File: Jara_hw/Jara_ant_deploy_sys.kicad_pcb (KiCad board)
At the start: 2 copper layers, 80 x 80 mm, 16 parts, among them J2 Conn_01x15, J3 Conn_01x10, Q1 Q_NMOS_GSD, Q2 Q_NMOS_GSD, SW3 SW_SPDT_312, SW4 SW_SPDT_312, U2 RFM95W-868S2

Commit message: Jennie and Jára PCBs prepared for manufacturing(?)
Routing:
- net (no net): vias 14 -> 17
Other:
- board text added: "NDE-JARA-ANT-DEPL-MECH:BOTTOM"
- board text added: "NDE-JARA-ANT-DEPL-MECH:TOP"
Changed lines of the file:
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@@
 		(pad_to_mask_clearance 0)
 		(allow_soldermask_bridges_in_footprints no)
+		(aux_axis_origin 114 54)
 		(pcbplotparams
 			(layerselection 0x00010fc_ffffffff)
@@
 			)
 		)
+		(model "C:/Users/Uživatel/Documents/MPA-NDE/kicad_project_libs/moment_switch/ZMA00A080L04RC.stp"
+			(offset
+				(xyz 0 0 0)
+			)
+			(scale
+				(xyz 1 1 1)
+			)
+			(rotate
+				(xyz 0 0 0)
+			)
+		)
 	)
 	(footprint "Connector_PinHeader_2.54mm:PinHeader_1x10_P2.54mm_Vertical"
@@
 			)
 		)
+		(model "C:/Users/Uživatel/Documents/MPA-NDE/kicad_project_libs/moment_switch/ZMA00A080L04RC.stp"
+			(offset
+				(xyz 0 0 0)
+			)
+			(scale
+				(xyz 1 1 1)
+			)
+			(rotate
+				(xyz 0 0 0)
+			)
+		)
 	)
 	(footprint "Package_TO_SOT_SMD:SOT-23"
@@
 			)
 		)
+		(model "C:/Users/Uživatel/Documents/MPA-NDE/kicad_project_libs/hoperf95/RFM95 LoRa v15.step"
+			(offset
+				(xyz 8 -8 0)
+			)
+			(scale
+				(xyz 1 1 1)
+			)
+			(rotate
+				(xyz -90 0 -180)
+			)
+		)
 	)
 	(footprint "Resistor_SMD:R_0805_2012Metric"
@@
 	)
 	(gr_line
+		(start 195.36 135.35)
+		(end 195.36 130.83)
+		(stroke
+			(width 0.6)
+			(type default)
+		)
+		(layer "Dwgs.User")
+	)
+	(gr_line
 		(start 149.6 102.25)
 		(end 147.85 102.99)
@@
 	)
 	(gr_line
+		(start 114.62 130.64)
+		(end 114.62 135.39)
+		(stroke
+			(width 0.6)
+			(type default)
+		)
+		(layer "Dwgs.User")
+	)
+	(gr_line
 		(start 147.85 102.99)
 		(end 147.33 103.07)
@@
 	)
 	(gr_line
+		(start 195.39 54.62)
+		(end 190.87 54.62)
+		(stroke
+			(width 0.6)
+			(type default)
+		)
+		(layer "Dwgs.User")
+	)
+	(gr_line
 		(start 194.49 87.16)
 		(end 194.97 87.16)
@@
 	)
 	(gr_line
+		(start 114.62 135.39)
+		(end 119.14 135.39)
+		(stroke
+			(width 0.6)
+			(type default)
+		)
+		(layer "Dwgs.User")
+	)
+	(gr_line
 		(start 162.1 117.8)
 		(end 160.43 114.67)
@@
 	)
 	(gr_line
+		(start 190.61 135.35)
+		(end 195.36 135.35)
+		(stroke
+			(width 0.6)
+			(type default)
+		)
+		(layer "Dwgs.User")
+	)
+	(gr_line
 		(start 165.08 121.54)
 		(end 162.1 117.8)
@@
 	)
 	(gr_line
+		(start 195.39 59.37)
+		(end 195.39 54.62)
+		(stroke
+			(width 0.6)
+			(type default)
+		)
+		(layer "Dwgs.User")
+	)
+	(gr_line
 		(start 151.21 81.48)
 		(end 151.2 99.08)
@@
 	)
 	(gr_line
+		(start 114.64 54.64)
+		(end 114.64 59.16)
+		(stroke
+			(width 0.6)
+			(type default)
+		)
+		(layer "Dwgs.User")
+	)
+	(gr_line
 		(start 160.27 87.99)
 		(end 162.02 87.25)
@@
 	)
 	(gr_line
+		(start 119.39 54.64)
+		(end 114.64 54.64)
+		(stroke
+			(width 0.6)
+			(type default)
+		)
+		(layer "Dwgs.User")
+	)
+	(gr_line
 		(start 174.2 127.26)
 		(end 168.97 124.77)
@@
 		)
 	)
+	(gr_text "NDE-JARA-ANT-DEPL-MECH:TOP"
+		(at 141.74 53.67 0)
+		(layer "F.Cu")
+		(effects
+			(font
+				(size 1.5 1.5)
+				(thickness 0.375)
+				(bold yes)
+			)
+			(justify left bottom)
+		)
+	)
+	(gr_text "NDE-JARA-ANT-DEPL-MECH:BOTTOM"
+		(at 181.54 51.3 -0)
+		(layer "B.Cu")
+		(effects
+			(font
+				(size 1.5 1.5)
+				(thickness 0.375)
+				(bold yes)
+			)
+			(justify left bottom mirror)
+		)
+	)
+	(dimension
+		(type center)
+		(layer "Dwgs.User")
+		(pts
+			(xy 196 54) (xy 196 58.77)
+		)
+		(style
+			(thickness 1)
+			(arrow_length 1.27)
+			(text_position_mode 0)
+			(extension_offset 0.5) keep_text_aligned)
+	)
+	(dimension
+		(type center)
+		(layer "Dwgs.User")
+		(pts
+			(xy 114 54) (xy 114 58.94)
+		)
+		(style
+			(thickness 1)
+			(arrow_length 1.27)
+			(text_position_mode 0)
+			(extension_offset 0.5) keep_text_aligned)
+	)
+	(dimension
+		(type center)
+		(layer "Dwgs.User")
+		(pts
+			(xy 114 136) (xy 114 140.4)
+		)
+		(style
+			(thickness 1)
+			(arrow_length 1.27)
+			(text_position_mode 0)
+			(extension_offset 0.5) keep_text_aligned)
+	)
 	(via
 		(at 144.5 97.91)
@@
 	)
 	(via
+		(at 114 54)
+		(size 1)
+		(drill 0.6)
+		(layers "F.Cu" "B.Cu")
+		(net 0)
+	)
+	(via
 		(at 166.56 116.54)
 		(size 4.5)
@@
 	)
 	(via
+		(at 196 54)
+		(size 1)
+		(drill 0.6)
+		(layers "F.Cu" "B.Cu")
+		(net 0)
+	)
+	(via
 		(at 191 91.09)
 		(size 4.5)
@@
 		(layers "F.Cu" "B.Cu")
 		(net 0)
+	)
+	(via
+		(at 114 136)
+		(size 1)
+		(drill 0.6)
+		(layers "F.Cu" "B.Cu")
+		(net 0)

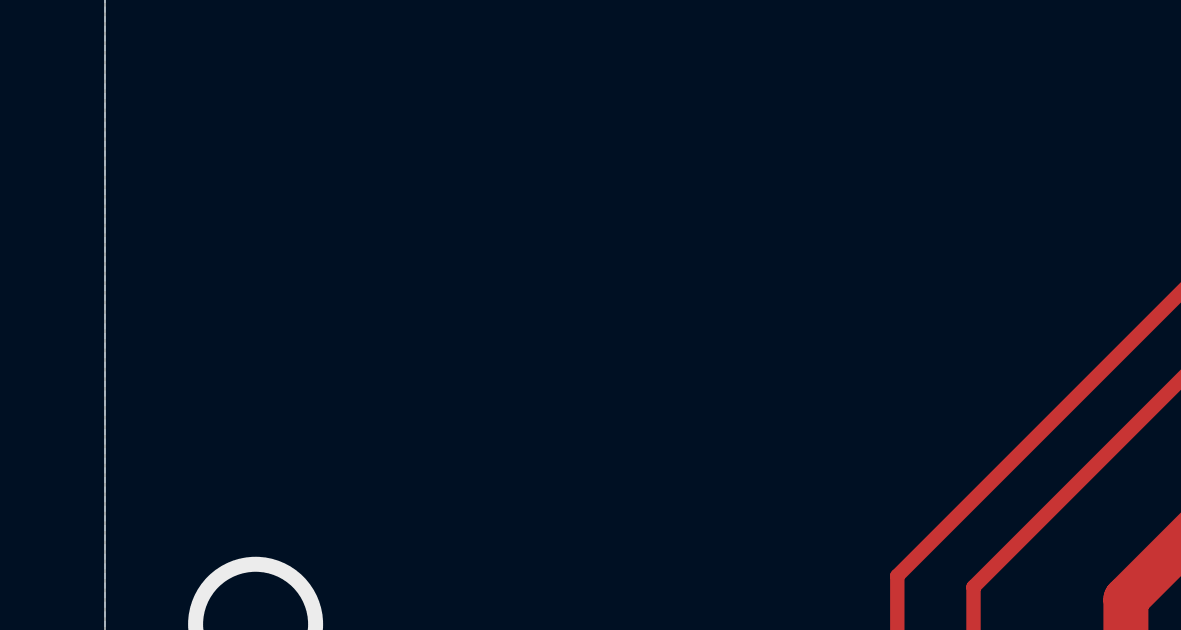
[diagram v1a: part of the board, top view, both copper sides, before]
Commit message: 3D models of Jára and Jennie PCBs added
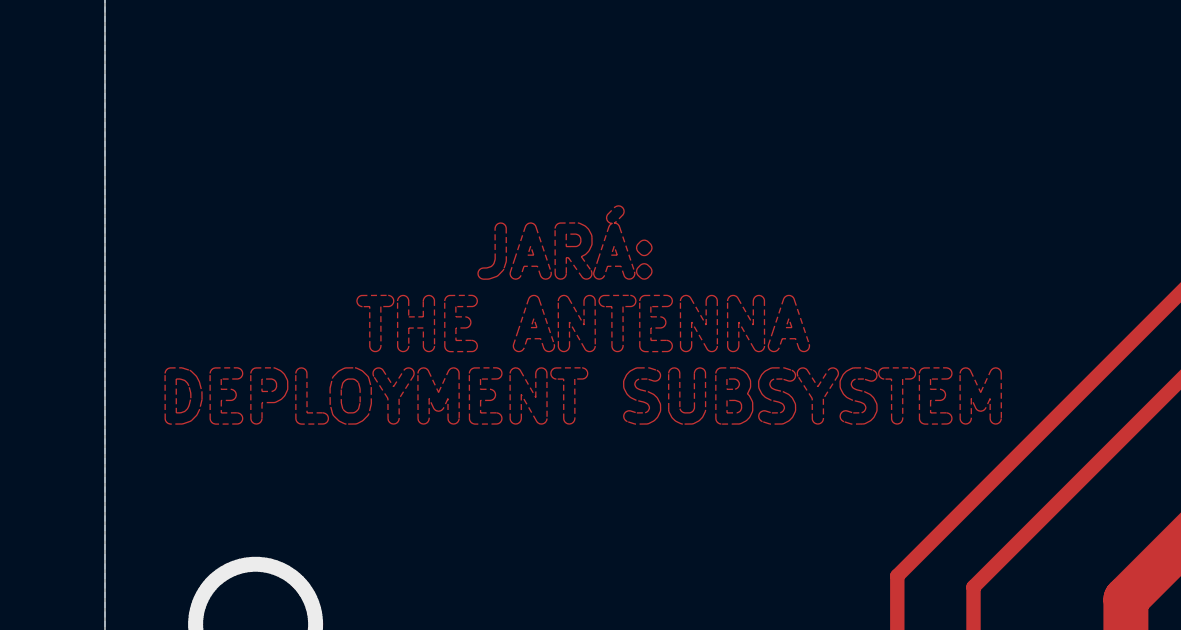
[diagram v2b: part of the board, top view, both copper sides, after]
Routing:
- added copper zone on F.Cu, net (none)

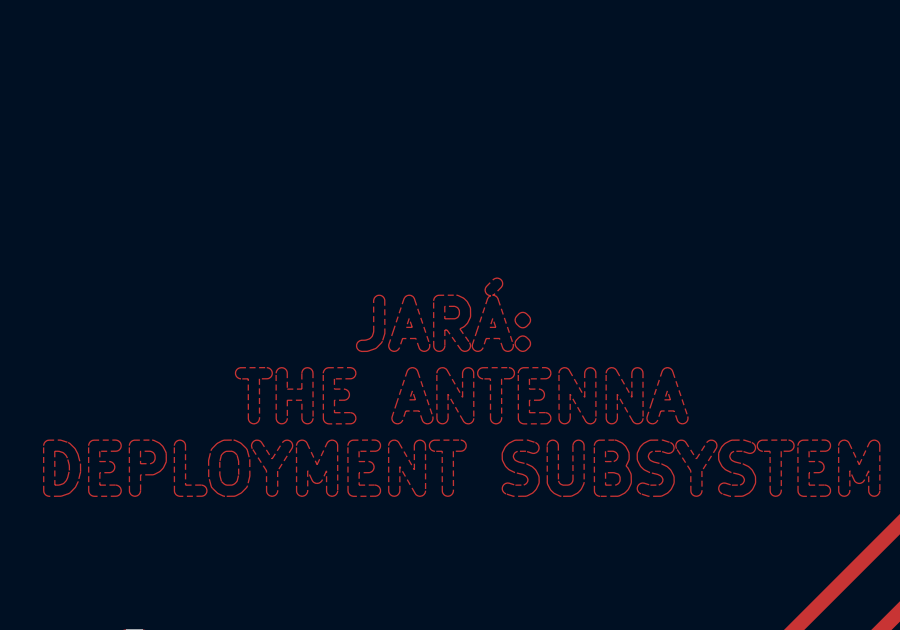
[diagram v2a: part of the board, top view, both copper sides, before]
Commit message: small fix of small routing error on Jennie PCB (V_batt routed to different pins on pinheader to maintain compatibility with Jára pinheader)
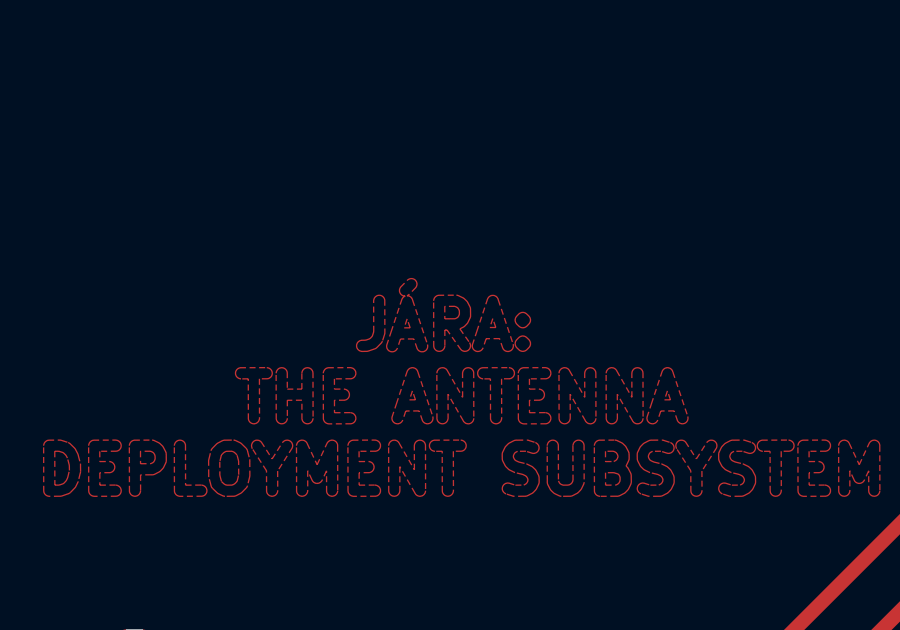
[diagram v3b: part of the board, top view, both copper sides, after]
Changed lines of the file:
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@@
 		(polygon
 			(pts
-				(xy 129.226158 116.61772) (xy 129.239523 116.61867) (xy 129.260554 116.629185) (xy 129.282855 116.636619)
-				(xy 129.292974 116.645395) (xy 129.30496 116.651388) (xy 129.320363 116.669148) (xy 129.338124 116.684552)
-				(xy 129.344116 116.696537) (xy 129.352893 116.706657) (xy 129.360494 116.729294) (xy 129.370842 116.749989)
-				(xy 129.371753 116.762822) (xy 129.867878 118.240219) (xy 129.876027 118.276061) (xy 129.870842 118.349035)
-				(xy 129.838124 118.414472) (xy 129.782855 118.462405) (xy 129.713452 118.485539) (xy 129.640477 118.480354)
-				(xy 129.575041 118.447636) (xy 129.527107 118.392367) (xy 129.414034 118.055652) (xy 128.96747 118.057795)
-				(xy 128.867878 118.358805) (xy 128.852893 118.392367) (xy 128.80496 118.447636) (xy 128.739523 118.480354)
-				(xy 128.666549 118.485539) (xy 128.597145 118.462405) (xy 128.541876 118.414472) (xy 128.509158 118.349035)
-				(xy 128.503973 118.276061) (xy 128.64896 117.837848) (xy 128.64896 117.834362) (xy 128.654693 117.82052)
-				(xy 129.012122 116.740219) (xy 129.027107 116.706657) (xy 129.035883 116.696537) (xy 129.041876 116.684552)
-				(xy 129.059639 116.669146) (xy 129.075041 116.651388) (xy 129.087024 116.645396) (xy 129.097145 116.636619)
-				(xy 129.119445 116.629185) (xy 129.140477 116.61867) (xy 129.153842 116.61772) (xy 129.166549 116.613485)
-				(xy 129.19 116.615151) (xy 129.213452 116.613485)
-			)
-		)
-		(polygon
-			(pts
-				(xy 129.090604 117.685631) (xy 129.289457 117.684677) (xy 129.189451 117.386871)
+				(xy 132.012124 116.622068) (xy 132.025489 116.623018) (xy 132.04652 116.633533) (xy 132.068821 116.640967)
+				(xy 132.07894 116.649743) (xy 132.090926 116.655736) (xy 132.106329 116.673496) (xy 132.12409 116.6889)
+				(xy 132.130082 116.700885) (xy 132.138859 116.711005) (xy 132.14646 116.733642) (xy 132.156808 116.754337)
+				(xy 132.157719 116.76717) (xy 132.653844 118.244567) (xy 132.661993 118.280409) (xy 132.656808 118.353383)
+				(xy 132.62409 118.41882) (xy 132.568821 118.466753) (xy 132.499418 118.489887) (xy 132.426443 118.484702)
+				(xy 132.361007 118.451984) (xy 132.313073 118.396715) (xy 132.2 118.06) (xy 131.753436 118.062143)
+				(xy 131.653844 118.363153) (xy 131.638859 118.396715) (xy 131.590926 118.451984) (xy 131.525489 118.484702)
+				(xy 131.452515 118.489887) (xy 131.383111 118.466753) (xy 131.327842 118.41882) (xy 131.295124 118.353383)
+				(xy 131.289939 118.280409) (xy 131.434926 117.842196) (xy 131.434926 117.83871) (xy 131.440659 117.824868)
+				(xy 131.798088 116.744567) (xy 131.813073 116.711005) (xy 131.821849 116.700885) (xy 131.827842 116.6889)
+				(xy 131.845605 116.673494) (xy 131.861007 116.655736) (xy 131.87299 116.649744) (xy 131.883111 116.640967)
+				(xy 131.905411 116.633533) (xy 131.926443 116.623018) (xy 131.939808 116.622068) (xy 131.952515 116.617833)
+				(xy 131.975966 116.619499) (xy 131.999418 116.617833)
+			)
+		)
+		(polygon
+			(pts
+				(xy 131.87657 117.689979) (xy 132.075423 117.689025) (xy 131.975417 117.391219)
 			)
 		)
@@
 		(polygon
 			(pts
-				(xy 132.222741 116.072184) (xy 132.274471 116.123915) (xy 132.302468 116.191505) (xy 132.302468 116.264665)
-				(xy 132.274471 116.332254) (xy 132.036867 116.574952) (xy 132.008454 116.598269) (xy 131.968871 116.614665)
-				(xy 131.975714 116.615151) (xy 131.999166 116.613485) (xy 132.011872 116.61772) (xy 132.025237 116.61867)
-				(xy 132.046268 116.629185) (xy 132.068569 116.636619) (xy 132.078688 116.645395) (xy 132.090674 116.651388)
-				(xy 132.106077 116.669148) (xy 132.123838 116.684552) (xy 132.12983 116.696537) (xy 132.138607 116.706657)
-				(xy 132.146208 116.729294) (xy 132.156556 116.749989) (xy 132.157467 116.762822) (xy 132.653592 118.240219)
-				(xy 132.661741 118.276061) (xy 132.656556 118.349035) (xy 132.623838 118.414472) (xy 132.568569 118.462405)
-				(xy 132.499166 118.485539) (xy 132.426191 118.480354) (xy 132.360755 118.447636) (xy 132.312821 118.392367)
-				(xy 132.199748 118.055652) (xy 131.753184 118.057795) (xy 131.653592 118.358805) (xy 131.638607 118.392367)
-				(xy 131.590674 118.447636) (xy 131.525237 118.480354) (xy 131.452263 118.485539) (xy 131.382859 118.462405)
-				(xy 131.32759 118.414472) (xy 131.294872 118.349035) (xy 131.289687 118.276061) (xy 131.434674 117.837848)
-				(xy 131.434674 117.834362) (xy 131.440407 117.82052) (xy 131.797836 116.740219) (xy 131.812821 116.706657)
-				(xy 131.821597 116.696537) (xy 131.82759 116.684552) (xy 131.845353 116.669146) (xy 131.860755 116.651388)
-				(xy 131.872738 116.645396) (xy 131.882859 116.636619) (xy 131.905159 116.629185) (xy 131.910999 116.626266)
-				(xy 131.867705 116.626266) (xy 131.800115 116.598269) (xy 131.748385 116.546538) (xy 131.720388 116.478949)
-				(xy 131.720388 116.405789) (xy 131.748385 116.338199) (xy 131.985988 116.095501) (xy 132.014401 116.072184)
-				(xy 132.081991 116.044187) (xy 132.155151 116.044187)
-			)
-		)
-		(polygon
-			(pts
-				(xy 131.876318 117.685631) (xy 132.075171 117.684677) (xy 131.975165 117.386871)
-			)
-		)
+				(xy 129.36757 116.087507) (xy 129.4193 116.139238) (xy 129.447297 116.206828) (xy 129.447297 116.279988)
+				(xy 129.4193 116.347577) (xy 129.181696 116.590275) (xy 129.153283 116.613592) (xy 129.1137 116.629988)
+				(xy 129.120543 116.630474) (xy 129.143995 116.628808) (xy 129.156701 116.633043) (xy 129.170066 116.633993)
+				(xy 129.191097 116.644508) (xy 129.213398 116.651942) (xy 129.223517 116.660718) (xy 129.235503 116.666711)
+				(xy 129.250906 116.684471) (xy 129.268667 116.699875) (xy 129.274659 116.71186) (xy 129.283436 116.72198)
+				(xy 129.291037 116.744617) (xy 129.301385 116.765312) (xy 129.302296 116.778145) (xy 129.798421 118.255542)
+				(xy 129.80657 118.291384) (xy 129.801385 118.364358) (xy 129.768667 118.429795) (xy 129.713398 118.477728)
+				(xy 129.643995 118.500862) (xy 129.57102 118.495677) (xy 129.505584 118.462959) (xy 129.45765 118.40769)
+				(xy 129.344577 118.070975) (xy 128.898013 118.073118) (xy 128.798421 118.374128) (xy 128.783436 118.40769)
+				(xy 128.735503 118.462959) (xy 128.670066 118.495677) (xy 128.597092 118.500862) (xy 128.527688 118.477728)
+				(xy 128.472419 118.429795) (xy 128.439701 118.364358) (xy 128.434516 118.291384) (xy 128.579503 117.853171)
+				(xy 128.579503 117.849685) (xy 128.585236 117.835843) (xy 128.942665 116.755542) (xy 128.95765 116.72198)
+				(xy 128.966426 116.71186) (xy 128.972419 116.699875) (xy 128.990182 116.684469) (xy 129.005584 116.666711)
+				(xy 129.017567 116.660719) (xy 129.027688 116.651942) (xy 129.049988 116.644508) (xy 129.055828 116.641589)
+				(xy 129.012534 116.641589) (xy 128.944944 116.613592) (xy 128.893214 116.561861) (xy 128.865217 116.494272)
+				(xy 128.865217 116.421112) (xy 128.893214 116.353522) (xy 129.130817 116.110824) (xy 129.15923 116.087507)
+				(xy 129.22682 116.05951) (xy 129.29998 116.05951)
+			)
+		)
+		(polygon
+			(pts
+				(xy 129.021147 117.700954) (xy 129.22 117.7) (xy 129.119994 117.402194)
+			)
+		)
